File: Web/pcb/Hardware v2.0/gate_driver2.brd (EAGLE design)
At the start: 49.2 x 55.9 mm, 25 parts, among them IC1 HCPL3120, IC2 HCPL3120

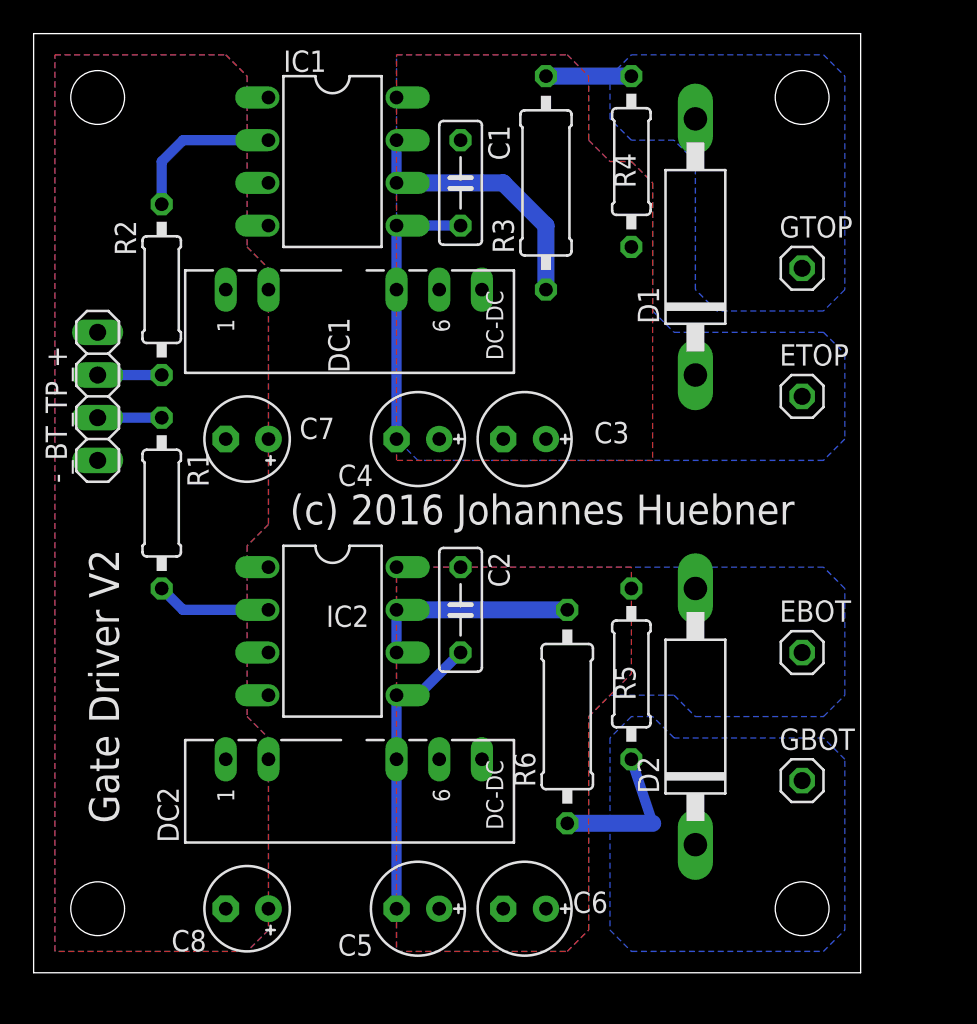
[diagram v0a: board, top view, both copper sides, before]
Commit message: added CAN info and temp detection
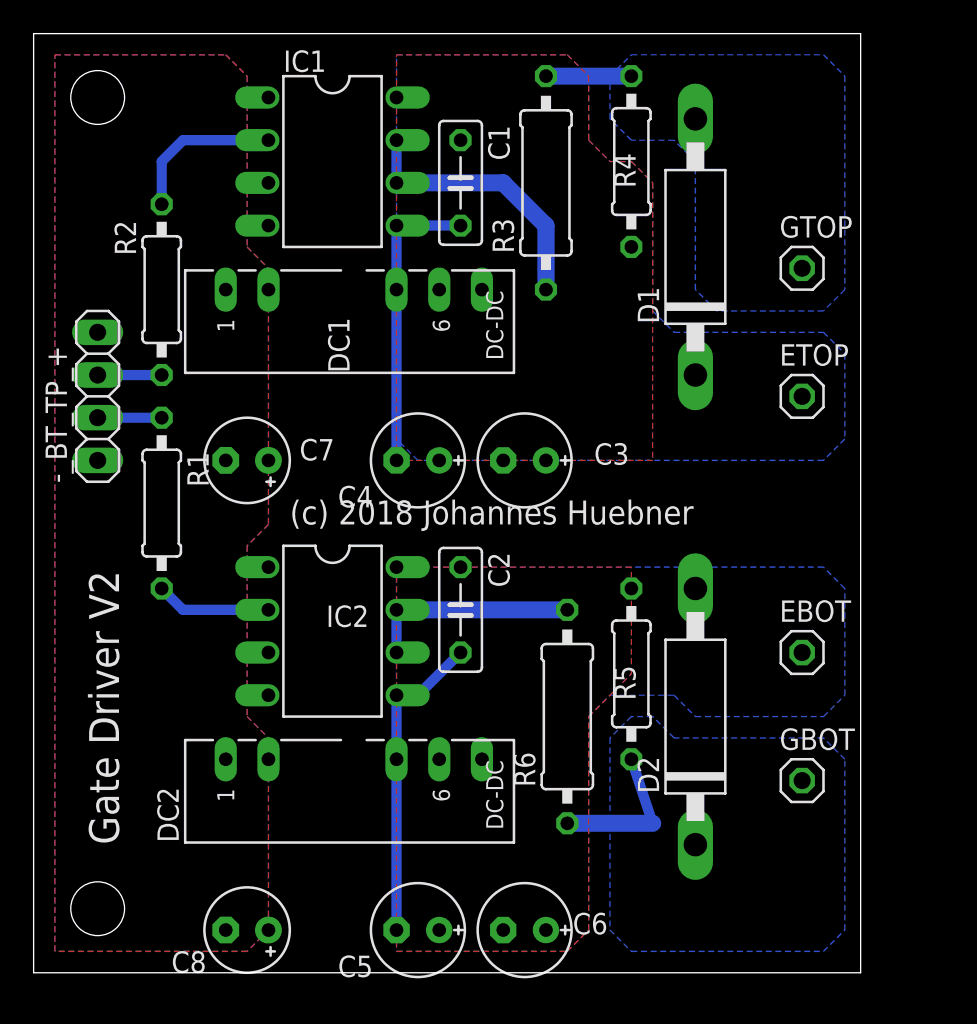
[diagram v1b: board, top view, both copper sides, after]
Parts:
- moved C5 1.27 mm to (22.9, 2.54)
- moved C6 1.27 mm to (29.2, 2.54)
- moved C8 1.27 mm to (12.7, 2.54)
- moved C3 1.27 mm to (29.2, 30.5)
- moved C4 1.27 mm to (22.9, 30.5)
- moved C7 1.27 mm to (12.7, 30.5)
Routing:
- net N$8: track 17.6 -> 18.8 mm
- net N$5: track 16.5 -> 17.8 mm
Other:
- board text added: "(c) 2018 Johannes Huebner"
- board text removed: "(c) 2016 Johannes Huebner"
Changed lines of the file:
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@@
 <?xml version="1.0" encoding="utf-8"?>
 <!DOCTYPE eagle SYSTEM "eagle.dtd">
-<eagle version="9.1.0">
+<eagle version="6.4">
 <drawing>
 <settings>
 <setting alwaysvectorfont="no"/>
-<setting keepoldvectorfont="yes"/>
 <setting verticaltext="up"/>
 </settings>
@@
 <wire x1="49.2" y1="55.87" x2="0" y2="55.87" width="0" layer="20"/>
 <wire x1="0" y1="55.87" x2="0" y2="0" width="0" layer="20"/>
-<text x="15.24" y="26.67" size="1.778" layer="25">(c) 2016 Johannes Huebner</text>
-<text x="5.08" y="8.89" size="1.778" layer="25" rot="R90">Gate Driver V2</text>
+<text x="15.24" y="26.67" size="1.4224" layer="25" font="vector">(c) 2018 Johannes Huebner</text>
+<text x="5.08" y="7.62" size="1.778" layer="25" rot="R90">Gate Driver V2</text>
 <hole x="3.81" y="52.07" drill="3.2"/>
 <hole x="3.81" y="3.81" drill="3.2"/>
-<hole x="45.72" y="52.07" drill="3.2"/>
-<hole x="45.72" y="3.81" drill="3.2"/>
 </plain>
 <attributes>
@@
 <param name="dpMaxLengthDifference" value="10mm"/>
 <param name="dpGapFactor" value="2.5"/>
+<param name="checkGrid" value="0"/>
 <param name="checkAngle" value="0"/>
 <param name="checkFont" value="1"/>
 <param name="checkRestrict" value="1"/>
-<param name="checkStop" value="0"/>
-<param name="checkValues" value="0"/>
-<param name="checkNames" value="1"/>
-<param name="checkWireStubs" value="1"/>
-<param name="checkPolygonWidth" value="0"/>
 <param name="useDiameter" value="13"/>
 <param name="maxErrors" value="50"/>
@@
 <pass name="Default">
 <param name="RoutingGrid" value="50mil"/>
-<param name="AutoGrid" value="1"/>
-<param name="Efforts" value="0"/>
-<param name="TopRouterVariant" value="1"/>
 <param name="tpViaShape" value="round"/>
 <param name="PrefDir.1" value="|"/>
@@
 <element name="C1" library="rcl" package="C050-025X075" value="100n" x="25.4" y="46.99" rot="R270"/>
 <element name="C2" library="rcl" package="C050-025X075" value="100n" x="25.4" y="21.59" rot="R270"/>
-<element name="C4" library="rcl" package="E2,5-6E" value="100µ" x="22.86" y="31.75" rot="R180"/>
-<element name="C5" library="rcl" package="E2,5-6E" value="100µ" x="22.86" y="3.81" rot="R180"/>
-<element name="C6" library="rcl" package="E2,5-6E" value="100µ" x="29.21" y="3.81" smashed="yes" rot="R180">
-<attribute name="NAME" x="34.163" y="4.826" size="1.27" layer="25" ratio="10" rot="R180"/>
-<attribute name="VALUE" x="26.543" y="6.35" size="1.27" layer="27" ratio="10" rot="R180"/>
+<element name="C4" library="rcl" package="E2,5-6E" value="100µ" x="22.86" y="30.48" rot="R180"/>
+<element name="C5" library="rcl" package="E2,5-6E" value="100µ" x="22.86" y="2.54" rot="R180"/>
+<element name="C6" library="rcl" package="E2,5-6E" value="100µ" x="29.21" y="2.54" smashed="yes" rot="R180">
+<attribute name="NAME" x="34.163" y="3.556" size="1.27" layer="25" ratio="10" rot="R180"/>
+<attribute name="VALUE" x="26.543" y="5.08" size="1.27" layer="27" ratio="10" rot="R180"/>
 </element>
 <element name="GTOP" library="pinhead" package="1X01" value="" x="45.72" y="41.91"/>
@@
 <element name="R6" library="rcl" package="0309/12" value="4R7" x="31.75" y="15.24" rot="R90"/>
 <element name="-_BT_TP_+" library="pinhead" package="1X04" value="" x="3.81" y="34.29" rot="R90"/>
-<element name="C7" library="rcl" package="E2,5-5" value="100µ" x="12.7" y="31.75" smashed="yes" rot="R180">
-<attribute name="NAME" x="17.907" y="33.02" size="1.27" layer="25" ratio="10" rot="R180"/>
-<attribute name="VALUE" x="10.287" y="34.163" size="1.27" layer="27" ratio="10" rot="R180"/>
-</element>
-<element name="C8" library="rcl" package="E2,5-5" value="100µ" x="12.7" y="3.81" rot="R180"/>
+<element name="C7" library="rcl" package="E2,5-5" value="100µ" x="12.7" y="30.48" smashed="yes" rot="R180">
+<attribute name="NAME" x="17.907" y="31.75" size="1.27" layer="25" ratio="10" rot="R180"/>
+<attribute name="VALUE" x="10.287" y="32.893" size="1.27" layer="27" ratio="10" rot="R180"/>
+</element>
+<element name="C8" library="rcl" package="E2,5-5" value="100µ" x="12.7" y="2.54" rot="R180"/>
 <element name="D1" library="diode" package="CB417-15" value="P6KEXXC" x="39.37" y="43.18" rot="R90"/>
 <element name="D2" library="diode" package="CB417-15" value="P6KEXXC" x="39.37" y="15.24" rot="R90"/>
-<element name="C3" library="rcl" package="E2,5-6E" value="100µ" x="29.21" y="31.75" smashed="yes" rot="R180">
-<attribute name="NAME" x="35.433" y="32.766" size="1.27" layer="25" ratio="10" rot="R180"/>
-<attribute name="VALUE" x="26.543" y="34.29" size="1.27" layer="27" ratio="10" rot="R180"/>
+<element name="C3" library="rcl" package="E2,5-6E" value="100µ" x="29.21" y="30.48" smashed="yes" rot="R180">
+<attribute name="NAME" x="35.433" y="31.496" size="1.27" layer="25" ratio="10" rot="R180"/>
+<attribute name="VALUE" x="26.543" y="33.02" size="1.27" layer="27" ratio="10" rot="R180"/>
 </element>
 </elements>
@@
 <contactref element="C1" pad="2"/>
 <contactref element="IC1" pad="5"/>
-<wire x1="21.59" y1="31.75" x2="21.59" y2="40.64" width="0.6096" layer="16"/>
+<wire x1="21.59" y1="30.48" x2="21.59" y2="40.64" width="0.6096" layer="16"/>
 <wire x1="21.59" y1="44.45" x2="25.4" y2="44.45" width="0.6096" layer="16"/>
 <wire x1="21.59" y1="40.64" x2="21.59" y2="44.45" width="0.6096" layer="16"/>
@@
 <contactref element="C2" pad="2"/>
 <contactref element="IC2" pad="5"/>
-<wire x1="21.59" y1="3.81" x2="21.59" y2="12.7" width="0.6096" layer="16"/>
+<wire x1="21.59" y1="2.54" x2="21.59" y2="12.7" width="0.6096" layer="16"/>
 <wire x1="21.59" y1="12.7" x2="21.59" y2="16.51" width="0.6096" layer="16"/>
 <wire x1="21.59" y1="16.51" x2="22.86" y2="16.51" width="0.6096" layer="16"/>
@@
 </signal>
 </signals>
-<mfgpreviewcolors>
-<mfgpreviewcolor name="soldermaskcolor" color="0xC8008000"/>
-<mfgpreviewcolor name="silkscreencolor" color="0xFFFEFEFE"/>
-<mfgpreviewcolor name="backgroundcolor" color="0xFF282828"/>
-<mfgpreviewcolor name="coppercolor" color="0xFFFFBF00"/>
-<mfgpreviewcolor name="substratecolor" color="0xFF786E46"/>
-</mfgpreviewcolors>
 </board>
 </drawing>
